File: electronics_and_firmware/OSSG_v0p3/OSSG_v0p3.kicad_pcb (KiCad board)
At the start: 4 copper layers, 85 x 9 mm, 69 parts, among them IC1 DW01A, J1 USB_B_Micro, J2 External PDM Mic Input, Q1 FS8205A, Q2 Q_NPN_BEC, Q3 Q_NPN_BEC, Q4 Q_PMOS_DGS, SW1 SW_SPST, U1 ESP32-PICO-D4, U2 TP4056, U3 XC6222B331MRG, U4 CH9102F, U5 CL7809SS, U6 CHIP_B02MM_STM

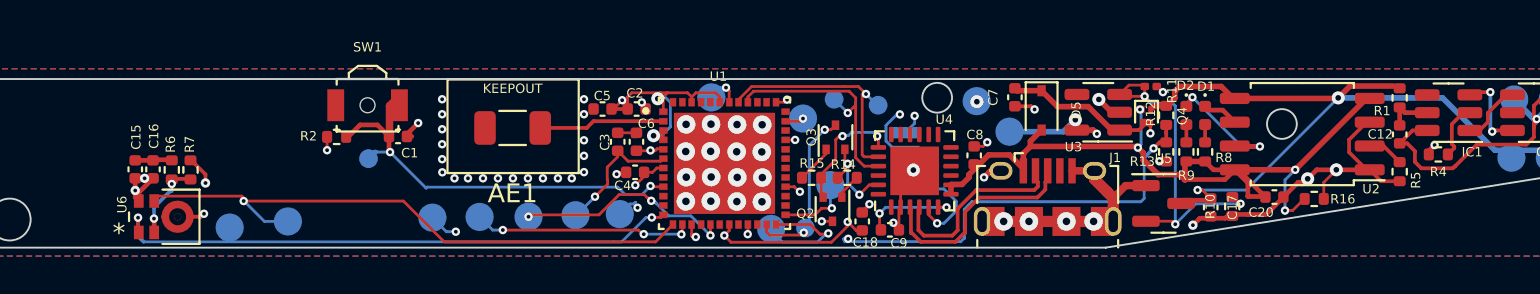
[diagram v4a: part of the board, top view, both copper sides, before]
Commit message: make breakout smaller, fix issues with breakouts too close to thermal pad, clean up silk screen, generate gerbers
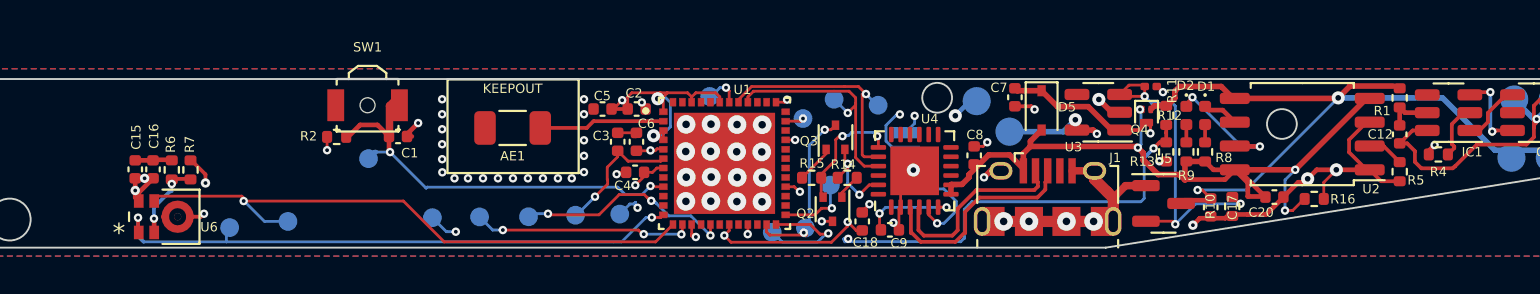
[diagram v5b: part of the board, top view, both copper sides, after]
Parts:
- TP1, TP10, TP11, TP19, TP2, TP20, TP21, TP22, TP24, TP6, TP7: footprint OSSG_footprints:Breakout_pads -> OSSG_footprints:Breakout_pads_small
- U6: value CHIP_B02MM_STM -> MP23DB01HPTR
- moved TP1 0.19 mm to (117.2, 83.2)
- moved TP19 0.10 mm to (113.9, 75.9)
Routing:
- net GND: track 47.3 -> 48.7 mm
- net IO32: track 30.6 -> 31.4 mm

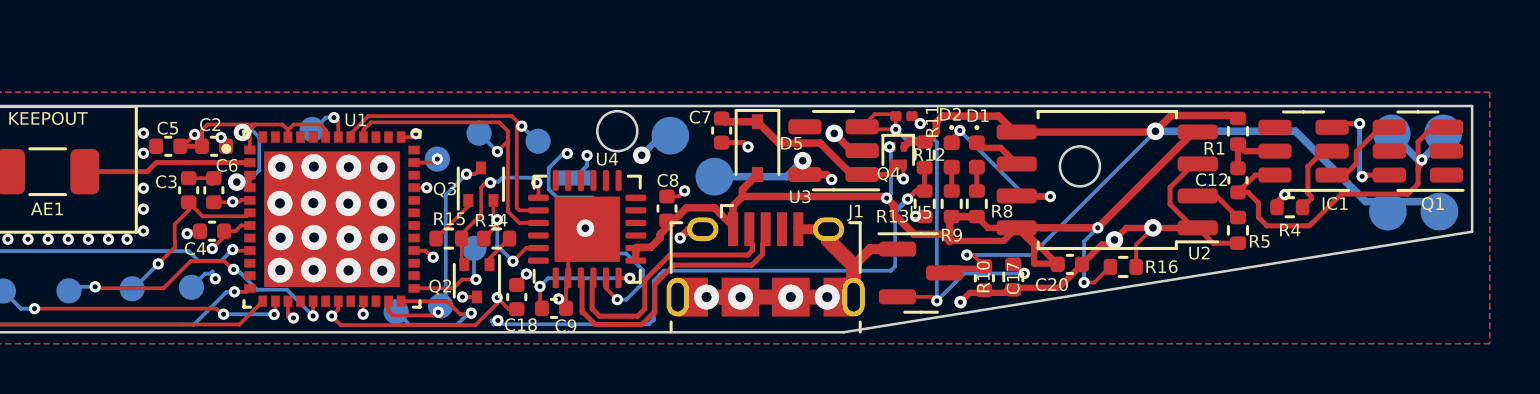
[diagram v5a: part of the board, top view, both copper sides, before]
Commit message: Fixed front silkscreen overlaps
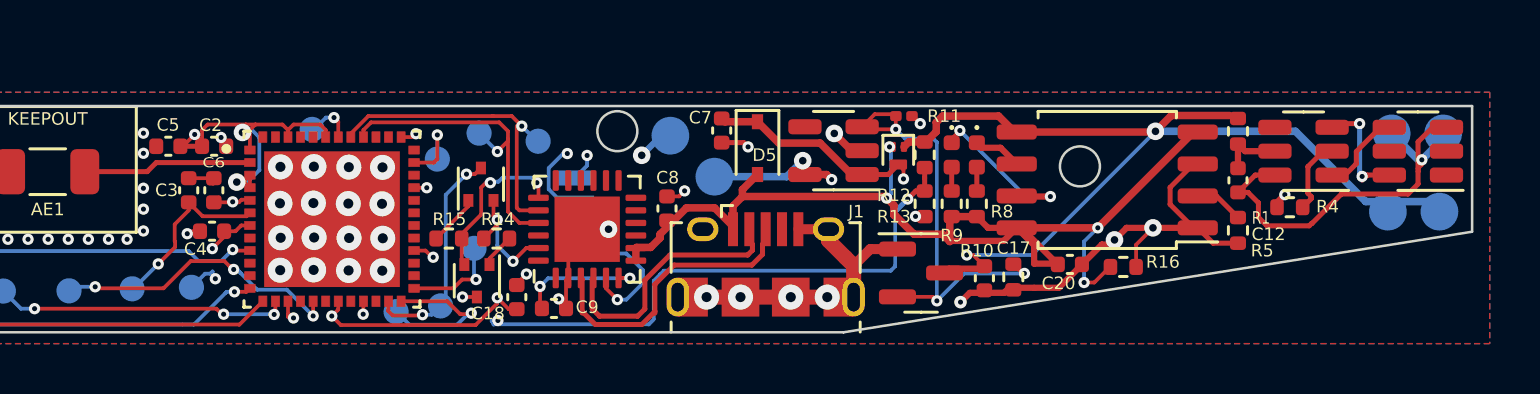
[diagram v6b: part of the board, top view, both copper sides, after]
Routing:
- net IO18: track 0.98 -> 2.90 mm
- net GND: track 48.7 -> 49.1 mm, vias 57 -> 56

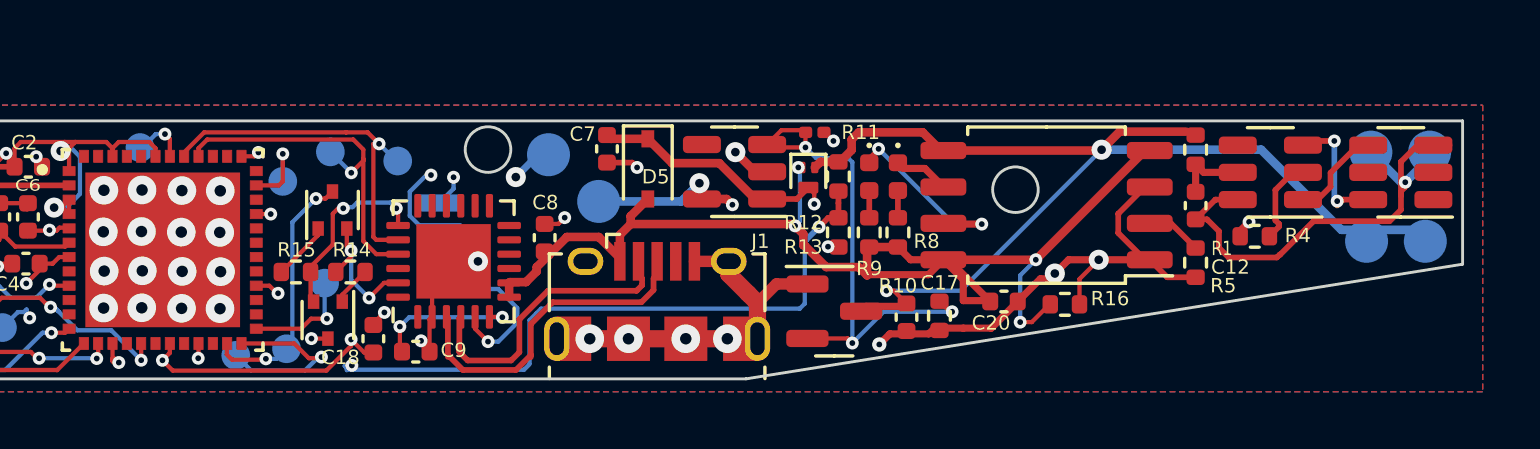
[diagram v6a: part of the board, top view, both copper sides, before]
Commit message: change to new LDO, change voltage supervisor, inspect board, slight silk screen changes
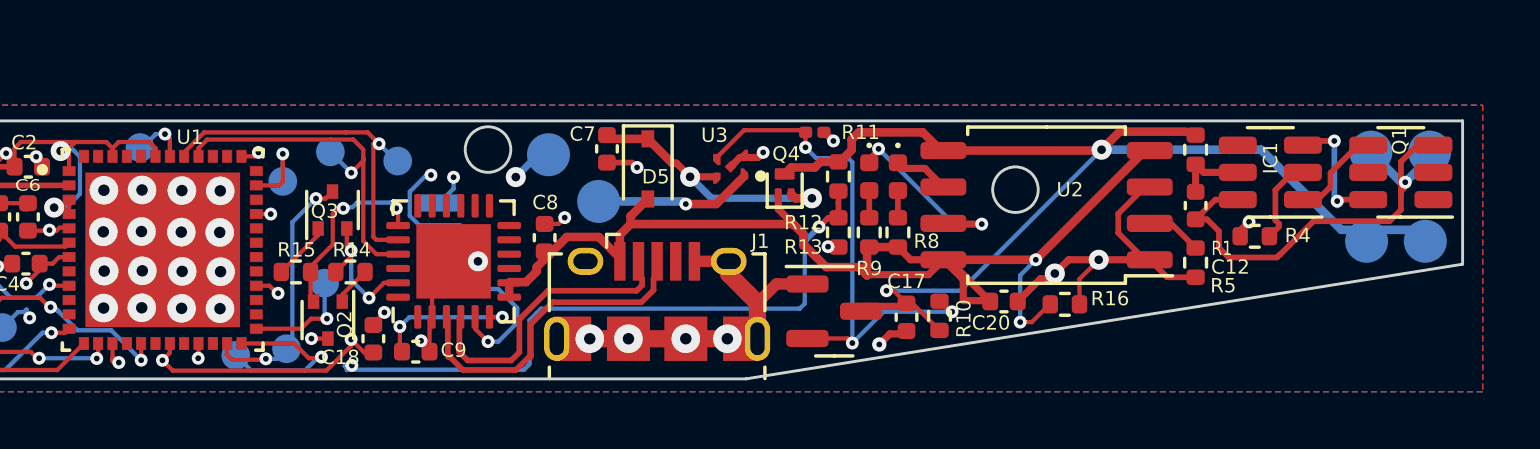
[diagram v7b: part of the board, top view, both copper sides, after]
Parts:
- Q4: value Q_PMOS_DGS -> Q_PMOS_GSD
- U3: value XC6222B331MRG -> NCP167BMX330TBG; footprint Package_TO_SOT_SMD:SOT-23-5 -> OSSG_footprints:REG_NCP167BMX330TBG
- U5: value CL7809SS -> XC61CC3002MR
- moved Q4 0.86 mm to (136.3, 77.2), turned to 90 degrees
- moved U3 0.22 mm to (134.5, 76.6)
- turned R10 to -90 degrees
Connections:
- Q4 pad 1: BATT+ -> V_USB
- Q4 pad 2: V_USB -> V_PSU
- Q4 pad 3: V_PSU -> BATT+
- R10 pad 1: GND -> PSEN
- R10 pad 2: PSEN -> BATT+
- U3 pad 1: V_PSU -> +3V3
- U3 pad 4: unconnected-(U3-Pad4) -> V_PSU
- U3 pad 5: +3V3 -> GND
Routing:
- net GND: track 49.1 -> 44.2 mm
- net BATT+: track 38.8 -> 41.4 mm
- net V_PSU: track 11.8 -> 13.3 mm, vias 2 -> 3
- net V_USB: track 43.7 -> 42.6 mm, vias 4 -> 2
- net PSEN: track 17.9 -> 18.4 mm
- net +3V3: track 27.0 -> 27.1 mm, vias 10 -> 9

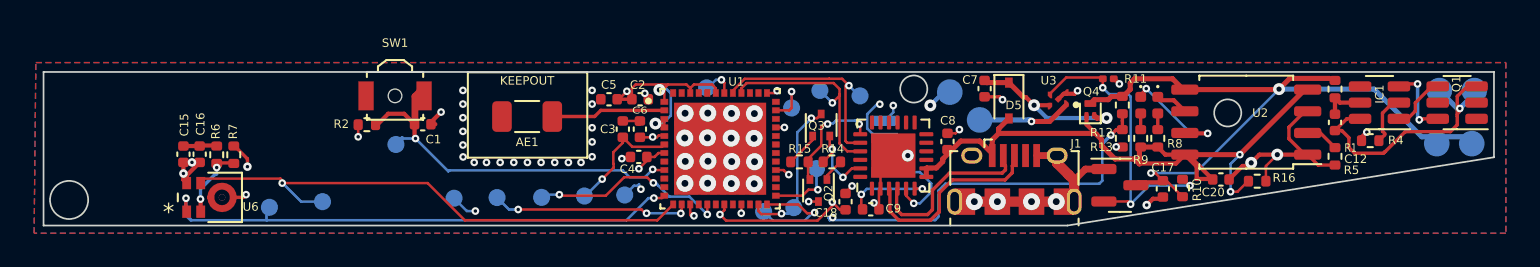
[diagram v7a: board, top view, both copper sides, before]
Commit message: change PICO gpios to use non-reserverd pins (and add reserved pins note), change FS8205A MPN to SOT-23 version, fix voltage supervisor symbol
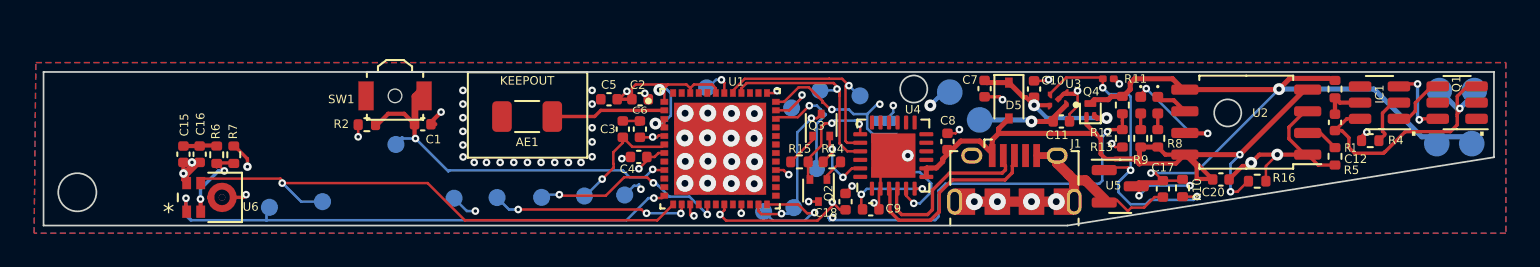
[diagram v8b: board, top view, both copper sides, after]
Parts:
- added C10: 1uF, Capacitor_SMD:C_0402_1005Metric, F.Cu at (133.1, 76.0)
- added C11: 1uF, Capacitor_SMD:C_0402_1005Metric, F.Cu at (134.7, 77.9)
- TP21: value IO16_BO -> IO5_BO
- moved U5 0.06 mm to (138.1, 81.7)
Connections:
- R10 pad 1: PSEN -> BATT+
- R10 pad 2: BATT+ -> PSEN
- TP21 pad 1: IO16 -> IO5
- U1 pad 25: IO16 -> unconnected-(U1-Pad25)
- U1 pad 27: IO17 -> unconnected-(U1-Pad27)
- U1 pad 32: IO7 -> unconnected-(U1-Pad32)
- U1 pad 33: EXT1_MIC_CLK -> unconnected-(U1-Pad33)
- U1 pad 36: IO23 -> EXT1_MIC_CLK
- U5 pad 1: GND -> PSEN
- U5 pad 2: PSEN -> GND
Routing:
- net IO5: track 0.00 -> 6.86 mm, vias 0 -> 1
- net GND: track 44.2 -> 50.6 mm
- net BATT+: track 41.4 -> 47.3 mm, vias 2 -> 4
- net IO16: track 3.88 -> 0.00 mm, vias 1 -> 0
- net PSEN: track 18.4 -> 19.4 mm
- net +3V3: track 27.1 -> 27.9 mm
- net Net-(R6-Pad1): track 4.32 -> 5.09 mm
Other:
- outline, holes or cut-outs redrawn
- board text added: "."
